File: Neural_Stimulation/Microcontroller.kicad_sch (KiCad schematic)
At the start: 1 part, among them U2 Adafruit_Feather_ESP32S3

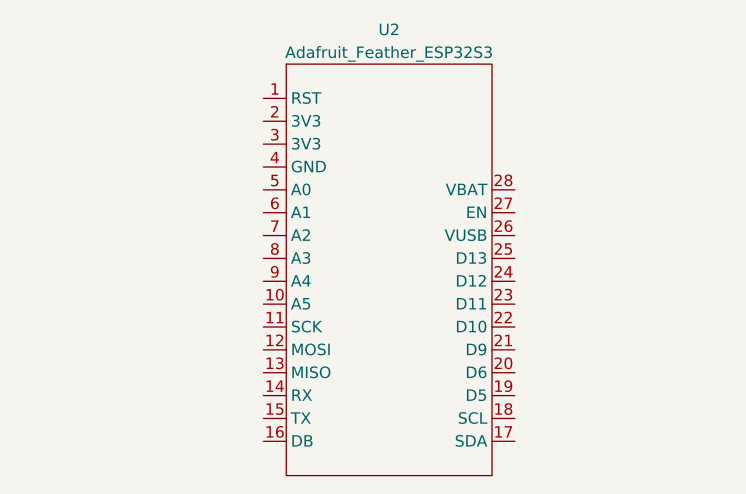
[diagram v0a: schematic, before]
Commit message: Added LDO
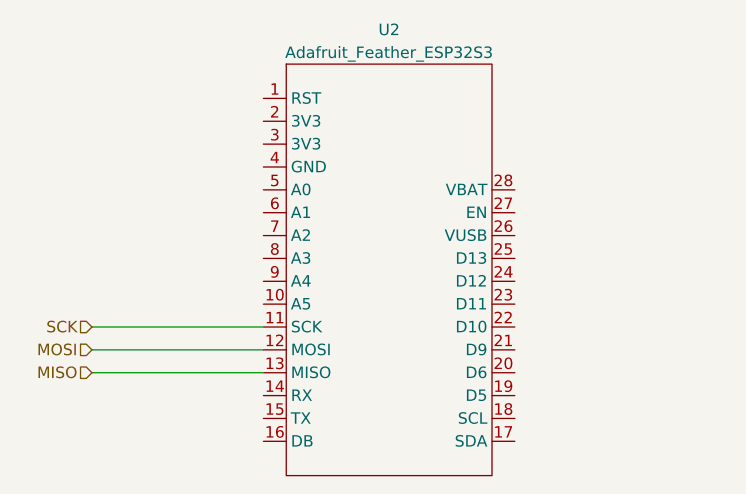
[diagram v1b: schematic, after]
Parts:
- U2: footprint (none) -> Adafruit_Feather_ESP32S3:Adafruit_Feather_ESP32S3
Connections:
- net SCK: now reaches U2.11 (SCK)
- net MOSI: now reaches U2.12 (MOSI)
- net MISO: now reaches U2.13 (MISO)
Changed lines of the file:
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@@
 	(generator_version "8.0")
 	(paper "A4")
+	(wire
+		(pts
+			(xy 104.14 97.79) (xy 123.19 97.79)
+		)
+		(stroke
+			(width 0)
+			(type default)
+		)
+	)
+	(wire
+		(pts
+			(xy 104.14 95.25) (xy 123.19 95.25)
+		)
+		(stroke
+			(width 0)
+			(type default)
+		)
+	)
+	(wire
+		(pts
+			(xy 104.14 100.33) (xy 123.19 100.33)
+		)
+		(stroke
+			(width 0)
+			(type default)
+		)
+	)
+	(hierarchical_label "MOSI"
+		(shape input)
+		(at 104.14 97.79 180)
+		(fields_autoplaced yes)
+		(effects
+			(font
+				(size 1.27 1.27)
+			)
+			(justify right)
+		)
+	)
+	(hierarchical_label "SCK"
+		(shape input)
+		(at 104.14 95.25 180)
+		(fields_autoplaced yes)
+		(effects
+			(font
+				(size 1.27 1.27)
+			)
+			(justify right)
+		)
+	)
+	(hierarchical_label "MISO"
+		(shape input)
+		(at 104.14 100.33 180)
+		(fields_autoplaced yes)
+		(effects
+			(font
+				(size 1.27 1.27)
+			)
+			(justify right)
+		)
+	)
 	(symbol
 		(lib_id "CSI040_stim:Adafruit_Feather_ESP32S3")
@@
 			)
 		)
-		(property "Footprint" ""
+		(property "Footprint" "Adafruit_Feather_ESP32S3:Adafruit_Feather_ESP32S3"
 			(at 137.16 88.9 0)
 			(effects

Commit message: Added level shifters
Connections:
- net CSN: now reaches U2.19 (D5)
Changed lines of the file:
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@@
+	(wire
+		(pts
+			(xy 151.13 102.87) (xy 163.83 102.87)
+		)
+		(stroke
+			(width 0)
+			(type default)
+		)
+	)
 	(wire
 		(pts
@@
 		)
 	)
+	(hierarchical_label "CSN"
+		(shape input)
+		(at 163.83 102.87 0)
+		(fields_autoplaced yes)
+		(effects
+			(font
+				(size 1.27 1.27)
+			)
+			(justify left)
+		)
+	)

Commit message: Added INT, TRIG, ATEST and RSTN pin circuits
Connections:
- net +3.3V: now reaches U2.2 (3V3)
- net +3.3V: now also U2.3 (3V3)
- net RSTN: now reaches U2.20 (D6)
- net INT: now reaches U2.21 (D9)
- net TRIG: now reaches U2.22 (D10)
- net CLK400K: now reaches U2.23 (D11)
- net GND: now reaches U2.4 (GND)
- net ATEST: now reaches U2.5 (A0)
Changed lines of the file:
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@@
 	(generator_version "8.0")
 	(paper "A4")
+	(junction
+		(at 118.11 72.39)
+		(diameter 0)
+		(color 0 0 0 0)
+	)
+	(wire
+		(pts
+			(xy 151.13 92.71) (xy 163.83 92.71)
+		)
+		(stroke
+			(width 0)
+			(type default)
+		)
+	)
 	(wire
 		(pts
@@
 	(wire
 		(pts
+			(xy 104.14 80.01) (xy 123.19 80.01)
+		)
+		(stroke
+			(width 0)
+			(type default)
+		)
+	)
+	(wire
+		(pts
+			(xy 151.13 95.25) (xy 163.83 95.25)
+		)
+		(stroke
+			(width 0)
+			(type default)
+		)
+	)
+	(wire
+		(pts
 			(xy 104.14 95.25) (xy 123.19 95.25)
 		)
@@
 	(wire
 		(pts
+			(xy 115.57 77.47) (xy 123.19 77.47)
+		)
+		(stroke
+			(width 0)
+			(type default)
+		)
+	)
+	(wire
+		(pts
 			(xy 104.14 100.33) (xy 123.19 100.33)
 		)
@@
 		)
 	)
+	(wire
+		(pts
+			(xy 109.22 72.39) (xy 118.11 72.39)
+		)
+		(stroke
+			(width 0)
+			(type default)
+		)
+	)
+	(wire
+		(pts
+			(xy 118.11 72.39) (xy 123.19 72.39)
+		)
+		(stroke
+			(width 0)
+			(type default)
+		)
+	)
+	(wire
+		(pts
+			(xy 123.19 74.93) (xy 118.11 74.93)
+		)
+		(stroke
+			(width 0)
+			(type default)
+		)
+	)
+	(wire
+		(pts
+			(xy 151.13 100.33) (xy 163.83 100.33)
+		)
+		(stroke
+			(width 0)
+			(type default)
+		)
+	)
+	(wire
+		(pts
+			(xy 118.11 74.93) (xy 118.11 72.39)
+		)
+		(stroke
+			(width 0)
+			(type default)
+		)
+	)
+	(wire
+		(pts
+			(xy 151.13 97.79) (xy 163.83 97.79)
+		)
+		(stroke
+			(width 0)
+			(type default)
+		)
+	)
+	(global_label "GND"
+		(shape input)
+		(at 115.57 77.47 180)
+		(fields_autoplaced yes)
+		(effects
+			(font
+				(size 1.27 1.27)
+			)
+			(justify right)
+		)
+		(property "Intersheetrefs" "${INTERSHEET_REFS}"
+			(at 108.7143 77.47 0)
+			(effects
+				(font
+					(size 1.27 1.27)
+				)
+				(justify right)
+				(hide yes)
+			)
+		)
+	)
 	(hierarchical_label "MOSI"
 		(shape input)
@@
 		)
 	)
+	(hierarchical_label "ATEST"
+		(shape input)
+		(at 104.14 80.01 180)
+		(fields_autoplaced yes)
+		(effects
+			(font
+				(size 1.27 1.27)
+			)
+			(justify right)
+		)
+	)
+	(hierarchical_label "CLK400K"
+		(shape input)
+		(at 163.83 92.71 0)
+		(fields_autoplaced yes)
+		(effects
+			(font
+				(size 1.27 1.27)
+			)
+			(justify left)
+		)
+	)
+	(hierarchical_label "TRIG"
+		(shape input)
+		(at 163.83 95.25 0)
+		(fields_autoplaced yes)
+		(effects
+			(font
+				(size 1.27 1.27)
+			)
+			(justify left)
+		)
+	)
+	(hierarchical_label "RSTN"
+		(shape input)
+		(at 163.83 100.33 0)
+		(fields_autoplaced yes)
+		(effects
+			(font
+				(size 1.27 1.27)
+			)
+			(justify left)
+		)
+	)
+	(hierarchical_label "INT"
+		(shape input)
+		(at 163.83 97.79 0)
+		(fields_autoplaced yes)
+		(effects
+			(font
+				(size 1.27 1.27)
+			)
+			(justify left)
+		)
+	)
 	(hierarchical_label "MISO"
 		(shape input)
@@
 		)
 	)
+	(symbol
+		(lib_id "power:+3.3V")
+		(at 109.22 72.39 90)
+		(unit 1)
+		(exclude_from_sim no)
+		(in_bom yes)
+		(on_board yes)
+		(dnp no)
+		(fields_autoplaced yes)
+		(property "Reference" "#PWR07"
+			(at 113.03 72.39 0)
+			(effects
+				(font
+					(size 1.27 1.27)
+				)
+				(hide yes)
+			)
+		)
+		(property "Value" "+3.3V"
+			(at 105.41 72.3899 90)
+			(effects
+				(font
+					(size 1.27 1.27)
+				)
+				(justify left)
+			)
+		)
+		(property "Footprint" ""
+			(at 109.22 72.39 0)
+			(effects
+				(font
+					(size 1.27 1.27)
+				)
+				(hide yes)
+			)
+		)
+		(property "Datasheet" ""
+			(at 109.22 72.39 0)
+			(effects
+				(font
+					(size 1.27 1.27)
+				)
+				(hide yes)
+			)
+		)
+		(property "Description" "Power symbol creates a global label with name \"+3.3V\""
+			(at 109.22 72.39 0)
+			(effects
+				(font
+					(size 1.27 1.27)
+				)
+				(hide yes)
+			)
+		)
+		(pin "1"
+		)
+		(instances
+			(project ""
+				(path "/0df850d8-90a2-4d89-b281-e26bc82d6cd9/3c0f2b06-344d-49ea-8124-93a4e51bdf5e"
+					(reference "#PWR07")
+					(unit 1)
+				)
+			)
+		)
+	)
